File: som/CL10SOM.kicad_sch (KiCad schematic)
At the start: 54 parts, among them IC1 10CL025YU256C8G, J1 Conn_01x02_Pin, U1 MT46H32M16LFBF-5 IT:C, U2 MX25L12833FM2, U6 AT93C46DN-SH-T, U7 SG3225CAN 50.0000M-TJGA6, X1 DF40C-120DS-0.4V51

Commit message: Use switching regulators for 3v3 and 1v2
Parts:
- removed C24, C25, C27: 2.2uF, Capacitor_SMD:C_0603_1608Metric, symbol Sheet1-altium-import:root_0_C_0805
- removed J1: Conn_01x02_Pin, Library:JUMPER_1, symbol Connector:Conn_01x02_Pin
- removed VR1, VR5: AP7366EA-33W5-7, Library:SOT95P285X140-5N, symbol Library:AP7366EA-33W5-7
- removed VR2: AP7366EA-12W5-7, Library:SOT95P285X140-5N, symbol Library:AP7366EA-12W5-7
- added C1, C2: GRM21BR60J226ME39L, Library:CAPC2012X140N, symbol Library:GRM21BR60J226ME39L
- added L1, L2: MURATA_DFE21CCN1R0MELL, Library:MURATA_DFE21CCN1R0MELL_0, symbol Library:MURATA_DFE21CCN1R0MELL
- added TP1, TP2, TP3: TestPoint, TestPoint:TestPoint_THTPad_D1.5mm_Drill0.7mm, symbol Connector:TestPoint
- added U3: SC189ZSKTRT, Library:SOT23-5-SC189_SEM, symbol Library:SC189ZSKTRT
- added U4: SC189CSKTRT, Library:SOT_CSKTRT_SEM, symbol Library:SC189CSKTRT
- C26, C99: value 2.2uF -> 4.7uF
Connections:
- net +3.3V is gone; now on net +3V3: X1.109, X1.111
- net +1V2: now also C2.1, L2.2, U4.4 (VOUT(1.2V))
- net +3V3: now also C28.2, C29.2, VR3.1 (IN), VR3.3 (EN), VR4.1 (IN), VR4.3 (EN), X1.11, X1.13, X1.15, X1.17, C1.1, L1.2, TP3.1, U3.4 (VOUT(3.3V))
- net +5V: now also C26.2, X1.9, TP2.1, U3.1 (VIN), U3.3 (EN), U4.1 (VIN), U4.3 (EN); no longer C28.2, C29.2, VR3.1 (IN), VR3.3 (EN), VR4.1 (IN), VR4.3 (EN)
- net GND: now also C1.2, C2.2, TP1.1, U3.2 (GND), U4.2 (GND)
- net TCK: now also X1.12; no longer X1.10
- net TDI: now also X1.10; no longer X1.9
- net TDO: now also X1.16; no longer X1.12
- net TMS: now also X1.14; no longer X1.11
- new net: L1.1, U3.5 (LX)
- new net: L2.1, U4.5 (LX)
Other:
- moved on the sheet: C22, C23, C26, C28, C29, C99, VR3, VR4

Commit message: All routed, no errors
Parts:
- removed U7: SG3225CAN 50.0000M-TJGA6, Library:SG3225CAN, symbol Sheet1-altium-import:root_0_SG-310
- added C10, C19, C24, C25, C27: 100nF, Capacitor_SMD:C_0603_1608Metric, symbol Sheet1-altium-import:root_1_C_0805
- added TP4, TP5, TP6: TestPoint, TestPoint:TestPoint_THTPad_D1.5mm_Drill0.7mm, symbol Connector:TestPoint
- added U7, U8: SG3225CAN 50.0000M-TJGA6, Library:SG3225CAN, symbol Library:SG3225CAN
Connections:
- net B7-CLK9 is gone; now on net GND: IC1.B9 (CLK9/DIFFCLK_5p)
- net B8-CLK10 is gone; now on net GND: IC1.A8 (CLK10/DIFFCLK_4n)
- net B8-CLK11 is gone; now on net GND: IC1.B8 (CLK11/DIFFCLK_4p)
- net +1V2: now also TP4.1
- net +1V8: now also X1.113, X1.115, C10.2, TP6.1, U8.4 (VCC); no longer X1.117, X1.119
- net +2V5: now also X1.109, X1.111, X1.17, TP5.1; no longer X1.113, X1.115
- net +3V3: now also X1.117, X1.119, X1.9, U7.4 (VCC); no longer X1.109, X1.111, X1.17
- net +5V: no longer X1.9
- net B3-IO15: no longer IC1.N8 (IO/DIFFIO_B11p), X1.54
- net B3-IO16: now also IC1.N8 (IO/DIFFIO_B11p), X1.54; no longer IC1.P8 (IO/DIFFIO_B12n), X1.56
- net CLC50: now also U7.3 (OUT)
- net GND: now also C10.1, C19.2, C24.2, C25.2, C27.2, U7.2 (GND), U8.2 (GND)
- net VCCB2: now also C19.1
- net VCCB3: now also C24.1
- net VCCB4: now also C25.1
- net VCCB5: now also C27.1
- net B7-CLK8 renamed CLCOPT
- net CLCOPT: now also U8.3 (OUT)
- new net B3-IO17: IC1.P8 (IO/DIFFIO_B12n), X1.56
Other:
- moved on the sheet: TP3

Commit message: Fixed warnings
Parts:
- removed TP2: TestPoint, TestPoint:TestPoint_THTPad_D1.5mm_Drill0.7mm, symbol Connector:TestPoint
- TP1, TP3, TP4, TP5, TP6: footprint TestPoint:TestPoint_THTPad_D1.5mm_Drill0.7mm -> TestPoint:TestPoint_THTPad_D1.0mm_Drill0.5mm
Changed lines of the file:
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@@
 	(wire
 		(pts
-			(xy 69.85 153.67) (xy 69.85 158.75)
-		)
-		(stroke
-			(width 0)
-			(type default)
-		)
-	)
-	(wire
-		(pts
 			(xy 203.2 378.46) (xy 203.2 379.73)
 		)
@@
 	(wire
 		(pts
-			(xy 55.88 153.67) (xy 55.88 158.75)
-		)
-		(stroke
-			(width 0)
-			(type default)
-		)
-	)
-	(wire
-		(pts
 			(xy 46.99 86.36) (xy 36.83 86.36)
 		)
@@
 	)
 	(symbol
-		(lib_id "Connector:TestPoint")
-		(at 55.88 158.75 180)
-		(unit 1)
-		(exclude_from_sim no)
-		(in_bom yes)
-		(on_board yes)
-		(dnp no)
-		(fields_autoplaced yes)
-		(property "Reference" "TP2"
-			(at 58.42 160.7819 0)
-			(effects
-				(font
-					(size 1.27 1.27)
-				)
-				(justify right)
-			)
-		)
-		(property "Value" "TestPoint"
-			(at 58.42 163.3219 0)
-			(effects
-				(font
-					(size 1.27 1.27)
-				)
-				(justify right)
-			)
-		)
-		(property "Footprint" "TestPoint:TestPoint_THTPad_D1.5mm_Drill0.7mm"
-			(at 50.8 158.75 0)
-			(effects
-				(font
-					(size 1.27 1.27)
-				)
-				(hide yes)
-			)
-		)
-		(property "Datasheet" "~"
-			(at 50.8 158.75 0)
-			(effects
-				(font
-					(size 1.27 1.27)
-				)
-				(hide yes)
-			)
-		)
-		(property "Description" "test point"
-			(at 55.88 158.75 0)
-			(effects
-				(font
-					(size 1.27 1.27)
-				)
-				(hide yes)
-			)
-		)
-		(pin "1"
-		)
-		(instances
-			(project ""
-				(path "/dc7b2672-e830-4a16-8d9e-d44ab4cff2d4"
-					(reference "TP2")
-					(unit 1)
-				)
-			)
-		)
-	)
-	(symbol
 		(lib_id "Sheet1-altium-import:root_1_C_0805")
 		(at 457.2 359.41 0)
@@
 			)
 		)
-		(property "Footprint" "TestPoint:TestPoint_THTPad_D1.5mm_Drill0.7mm"
+		(property "Footprint" "TestPoint:TestPoint_THTPad_D1.0mm_Drill0.5mm"
 			(at 45.72 154.94 0)
 			(effects
@@
 			)
 		)
-		(property "Footprint" "TestPoint:TestPoint_THTPad_D1.5mm_Drill0.7mm"
+		(property "Footprint" "TestPoint:TestPoint_THTPad_D1.0mm_Drill0.5mm"
 			(at 81.28 101.6 0)
 			(effects
@@
 	)
 	(symbol
-		(lib_id "power:+5V")
-		(at 55.88 153.67 0)
-		(unit 1)
-		(exclude_from_sim no)
-		(in_bom yes)
-		(on_board yes)
-		(dnp no)
-		(fields_autoplaced yes)
-		(property "Reference" "#PWR051"
-			(at 55.88 157.48 0)
-			(effects
-				(font
-					(size 1.27 1.27)
-				)
-				(hide yes)
-			)
-		)
-		(property "Value" "+5V"
-			(at 55.88 148.59 0)
-			(effects
-				(font
-					(size 1.27 1.27)
-				)
-			)
-		)
-		(property "Footprint" ""
-			(at 55.88 153.67 0)
-			(effects
-				(font
-					(size 1.27 1.27)
-				)
-				(hide yes)
-			)
-		)
-		(property "Datasheet" ""
-			(at 55.88 153.67 0)
-			(effects
-				(font
-					(size 1.27 1.27)
-				)
-				(hide yes)
-			)
-		)
-		(property "Description" "Power symbol creates a global label with name \"+5V\""
-			(at 55.88 153.67 0)
-			(effects
-				(font
-					(size 1.27 1.27)
-				)
-				(hide yes)
-			)
-		)
-		(pin "1"
-		)
-		(instances
-			(project "HyperFusionXC"
-				(path "/dc7b2672-e830-4a16-8d9e-d44ab4cff2d4"
-					(reference "#PWR051")
-					(unit 1)
-				)
-			)
-		)
-	)
-	(symbol
 		(lib_id "Sheet1-altium-import:root_1_C_0805")
 		(at 274.32 85.09 0)
@@
 			)
 		)
-		(property "Footprint" "TestPoint:TestPoint_THTPad_D1.5mm_Drill0.7mm"
+		(property "Footprint" "TestPoint:TestPoint_THTPad_D1.0mm_Drill0.5mm"
 			(at 128.27 41.91 0)
 			(effects
@@
 			)
 		)
-		(property "Footprint" "TestPoint:TestPoint_THTPad_D1.5mm_Drill0.7mm"
+		(property "Footprint" "TestPoint:TestPoint_THTPad_D1.0mm_Drill0.5mm"
 			(at 129.54 73.66 0)
 			(effects
@@
 			)
 		)
-		(property "Footprint" "TestPoint:TestPoint_THTPad_D1.5mm_Drill0.7mm"
+		(property "Footprint" "TestPoint:TestPoint_THTPad_D1.0mm_Drill0.5mm"
 			(at 81.28 127 0)
 			(effects

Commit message: Improvements
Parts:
- H1: footprint MountingHole:MountingHole_3.5mm_Pad_Via -> MountingHole:MountingHole_2.7mm_M2.5_Pad_Via
- IC1: footprint BGA256C80P16X16_1400X1400X150 -> Library:BGA256C80P16X16_1400X1400X150
- U1: footprint MIC-VFBGA-60-BF_MRN -> Library:MIC-VFBGA-60-BF_MRN
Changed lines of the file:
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@@
 			)
 		)
-		(property "Footprint" "MountingHole:MountingHole_3.5mm_Pad_Via"
+		(property "Footprint" "MountingHole:MountingHole_2.7mm_M2.5_Pad_Via"
 			(at 558.8 359.41 0)
 			(effects
@@
 			)
 		)
-		(property "Footprint" "MIC-VFBGA-60-BF_MRN"
+		(property "Footprint" "Library:MIC-VFBGA-60-BF_MRN"
 			(at 440.69 105.41 0)
 			(effects
@@
 			)
 		)
-		(property "Footprint" "BGA256C80P16X16_1400X1400X150"
+		(property "Footprint" "Library:BGA256C80P16X16_1400X1400X150"
 			(at 162.56 205.41 0)
 			(effects

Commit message: Improvements
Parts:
- C1, C2: LCSC (none) -> C77071
- C10: now not fitted
- C12, C13, C14, C15, C16, C17, C18, C19, C20, C21, C24, C25, C27, C30, C37, C38, C39, C40, C41, C42, C43, C45, C7, C9: LCSC (none) -> C45000
- C22, C23, C28, C29: LCSC (none) -> C100082
- C26, C99: DIGIKEY 1276-1134-1-ND -> 1276-2087-1-ND; LCSC (none) -> C107368
- IC1: LCSC (none) -> C1521917
- L1, L2: value MURATA_DFE21CCN1R0MELL -> DFE21CCN1R0MELL; LCSC (none) -> C3221768
- R44, R68: LCSC (none) -> C3029194
- R46, R47, R48, R49, R56, R58, R59, R60: LCSC (none) -> C238881
- R57: LCSC (none) -> C2484712
- R62: value 25E -> 24E9; DIGIKEY RMCF0603FT1K00CT-ND -> 311-24.9HRCT-ND; LCSC (none) -> C137759
- U1: LCSC (none) -> C2061960
- U2: LCSC (none) -> C701355
- U3: LCSC (none) -> C2650317
- U4: LCSC (none) -> C783594
- U6: LCSC (none) -> C6499
- U7: LCSC (none) -> C17330697
- U8: LCSC (none) -> C17330697; now not fitted
- X1: LCSC (none) -> C3647197

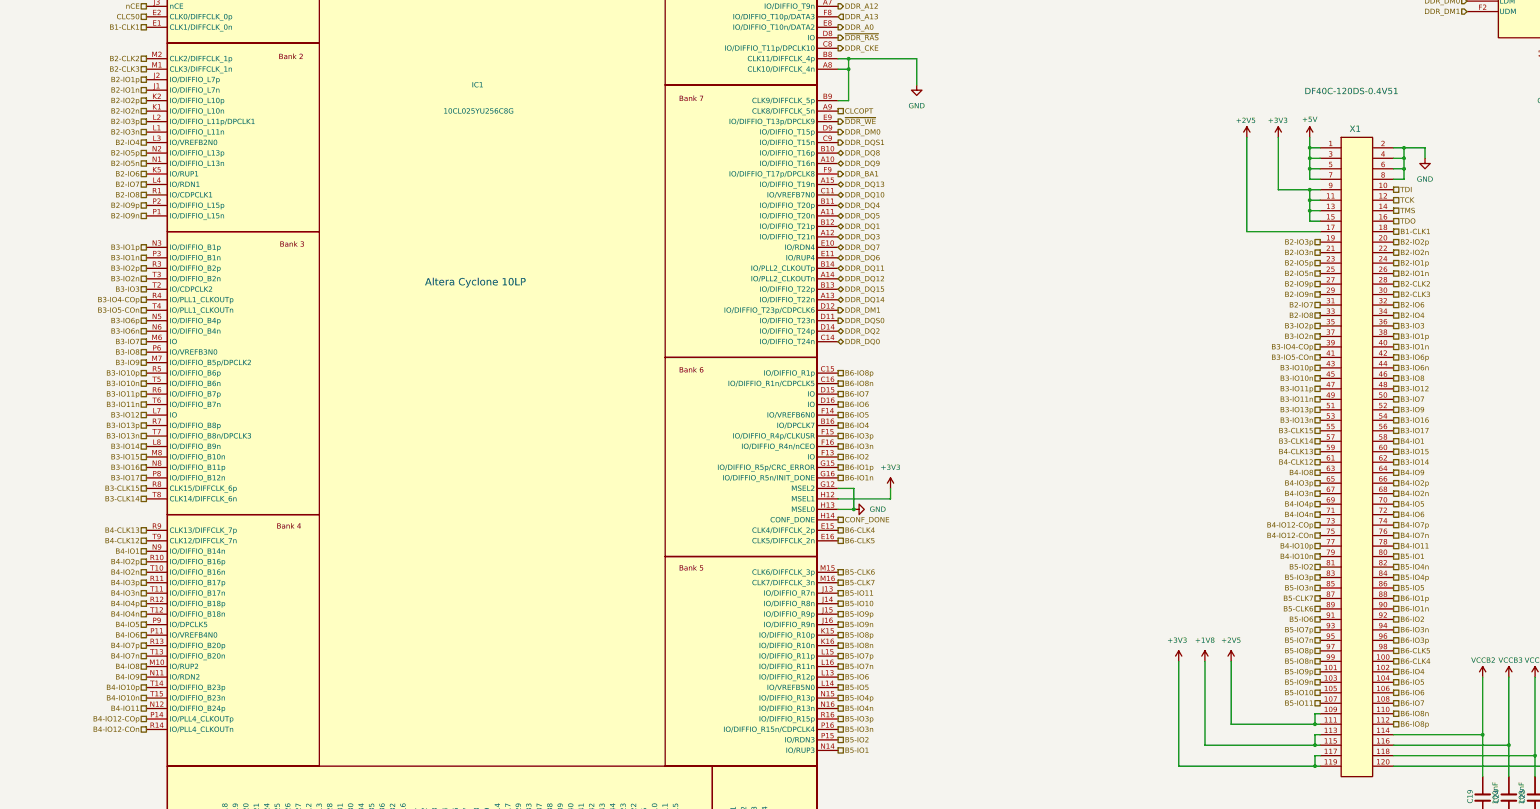
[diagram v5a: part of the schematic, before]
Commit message: Use differential routing
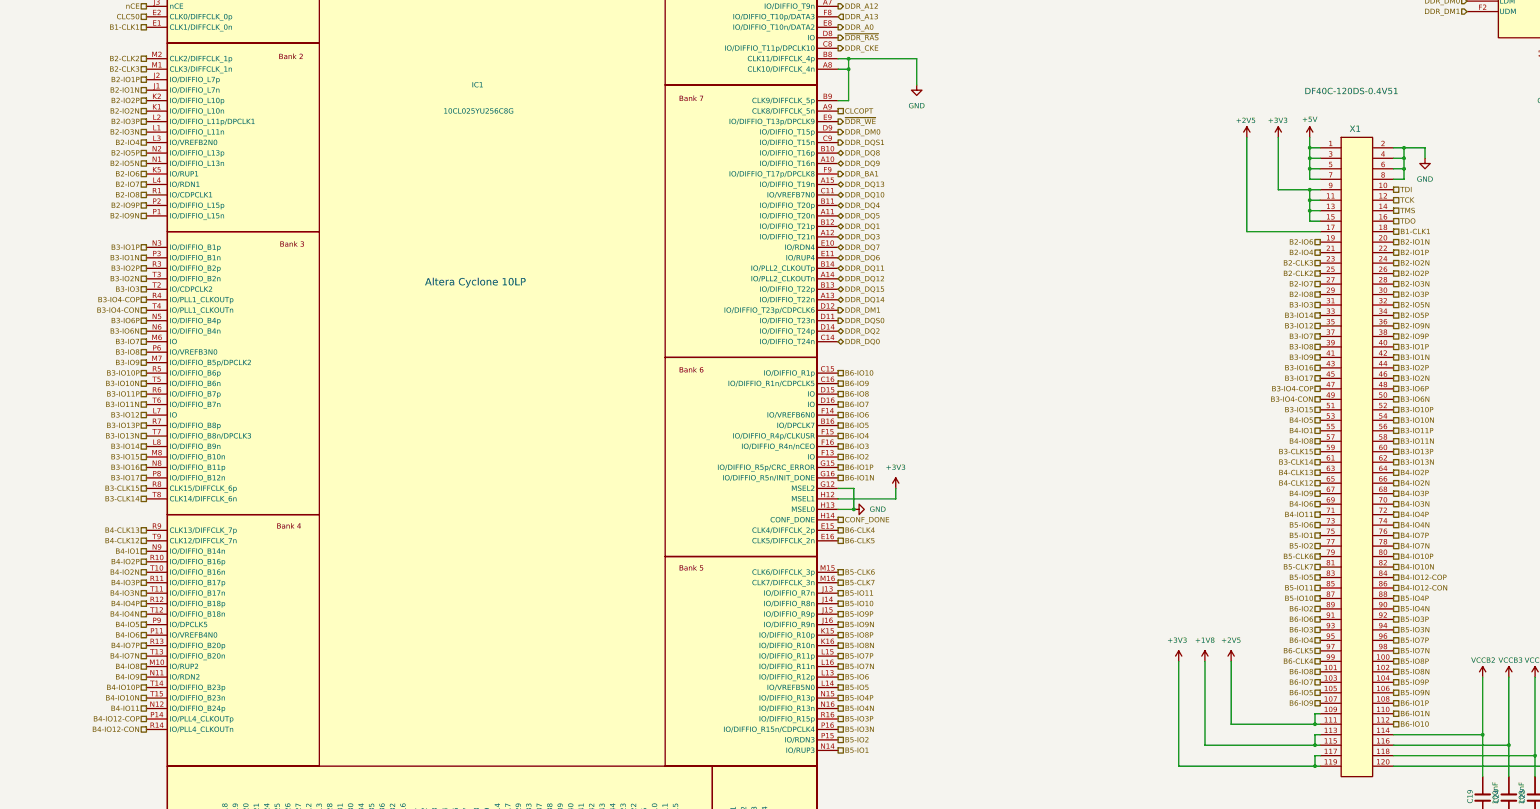
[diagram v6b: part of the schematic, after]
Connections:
- net B2-CLK2: now also X1.25; no longer X1.28
- net B2-CLK3: now also X1.23; no longer X1.30
- net B2-IO4: now also X1.21; no longer X1.34
- net B2-IO6: now also X1.19; no longer X1.32
- net B2-IO7: now also X1.27; no longer X1.31
- net B2-IO8: now also X1.29; no longer X1.33
- net B3-CLK14: now also X1.61; no longer X1.57
- net B3-CLK15: now also X1.59; no longer X1.55
- net B3-IO12: now also X1.35; no longer X1.48
- net B3-IO14: now also X1.33; no longer X1.62
- net B3-IO15: now also X1.51; no longer X1.60
- net B3-IO16: now also X1.43; no longer X1.54
- net B3-IO17: now also X1.45; no longer X1.56
- net B3-IO3: now also X1.31; no longer X1.36
- net B3-IO7: now also X1.37; no longer X1.50
- net B3-IO8: now also X1.39; no longer X1.46
- net B3-IO9: now also X1.41; no longer X1.52
- net B4-CLK12: now also X1.65; no longer X1.61
- net B4-CLK13: now also X1.63; no longer X1.59
- net B4-IO1: now also X1.55; no longer X1.58
- net B4-IO11: now also X1.71; no longer X1.78
- net B4-IO5: now also X1.53; no longer X1.70
- net B4-IO6: now also X1.69; no longer X1.72
- net B4-IO8: now also X1.57; no longer X1.63
- net B4-IO9: now also X1.67; no longer X1.64
- net B5-CLK6: now also X1.79; no longer X1.89
- net B5-CLK7: now also X1.81; no longer X1.87
- net B5-IO1: now also X1.75; no longer X1.80
- net B5-IO10: now also X1.87; no longer X1.105
- net B5-IO11: now also X1.85; no longer X1.107
- net B5-IO2: now also X1.77; no longer X1.81
- net B5-IO5: now also X1.83; no longer X1.86
- net B5-IO6: now also X1.73; no longer X1.91
- net B6-CLK4: now also X1.99; no longer X1.100
- net B6-CLK5: now also X1.97; no longer X1.98
- net B6-IO2: now also X1.89; no longer X1.92
- net B6-IO4: now also IC1.F15 (IO/DIFFIO_R4p/CLKUSR), X1.95; no longer IC1.B16 (IO/DPCLK7), X1.102
- net B6-IO5: now also IC1.B16 (IO/DPCLK7), X1.105; no longer IC1.F14 (IO/VREFB6N0), X1.104
- net B6-IO6: now also IC1.F14 (IO/VREFB6N0), X1.91; no longer IC1.D16 (IO), X1.106
- net B6-IO7: now also IC1.D16 (IO), X1.103; no longer IC1.D15 (IO), X1.108
- net B2-IO1n renamed B2-IO1N
- net B2-IO1N: now also X1.20; no longer X1.26
- net B2-IO1p renamed B2-IO1P
- net B2-IO1P: now also X1.22; no longer X1.24
- net B2-IO2n renamed B2-IO2N
- net B2-IO2N: now also X1.24; no longer X1.22
- net B2-IO2p renamed B2-IO2P
- net B2-IO2P: now also X1.26; no longer X1.20
- net B2-IO3n renamed B2-IO3N
- net B2-IO3N: now also X1.28; no longer X1.21
- net B2-IO3p renamed B2-IO3P
- net B2-IO3P: now also X1.30; no longer X1.19
- net B2-IO5n renamed B2-IO5N
- net B2-IO5N: now also X1.32; no longer X1.25
- net B2-IO5p renamed B2-IO5P
- net B2-IO5P: now also X1.34; no longer X1.23
- net B2-IO9n renamed B2-IO9N
- net B2-IO9N: now also X1.36; no longer X1.29
- net B2-IO9p renamed B2-IO9P
- net B2-IO9P: now also X1.38; no longer X1.27
- net B3-IO10n renamed B3-IO10N
- net B3-IO10N: now also X1.54; no longer X1.45
- net B3-IO10p renamed B3-IO10P
- net B3-IO10P: now also X1.52; no longer X1.43
- net B3-IO11n renamed B3-IO11N
- net B3-IO11N: now also X1.58; no longer X1.49
- net B3-IO11p renamed B3-IO11P
- net B3-IO11P: now also X1.56; no longer X1.47
- net B3-IO13n renamed B3-IO13N
- net B3-IO13N: now also X1.62; no longer X1.53
- net B3-IO13p renamed B3-IO13P
- net B3-IO13P: now also X1.60; no longer X1.51
- net B3-IO1n renamed B3-IO1N
- net B3-IO1N: now also X1.42; no longer X1.40
- net B3-IO1p renamed B3-IO1P
- net B3-IO1P: now also X1.40; no longer X1.38
- net B3-IO2n renamed B3-IO2N
- net B3-IO2N: now also X1.46; no longer X1.37
- net B3-IO2p renamed B3-IO2P
- net B3-IO2P: now also X1.44; no longer X1.35
- net B3-IO4-COp renamed B3-IO4-COP
- net B3-IO4-COP: now also X1.47; no longer X1.39
- net B3-IO5-COn renamed B3-IO4-CON
- net B3-IO4-CON: now also X1.49; no longer X1.41
- net B3-IO6n renamed B3-IO6N
- net B3-IO6N: now also X1.50; no longer X1.44
- net B3-IO6p renamed B3-IO6P
- net B3-IO6P: now also X1.48; no longer X1.42
- net B4-IO10n renamed B4-IO10N
- net B4-IO10N: now also X1.82; no longer X1.79
- net B4-IO10p renamed B4-IO10P
- net B4-IO10P: now also X1.80; no longer X1.77
- net B4-IO12-COn renamed B4-IO12-CON
- net B4-IO12-CON: now also X1.86; no longer X1.75
- net B4-IO12-COp renamed B4-IO12-COP
- net B4-IO12-COP: now also X1.84; no longer X1.73
- net B4-IO2n renamed B4-IO2N
- net B4-IO2N: now also X1.66; no longer X1.68
- net B4-IO2p renamed B4-IO2P
- net B4-IO2P: now also X1.64; no longer X1.66
- net B4-IO3n renamed B4-IO3N
- net B4-IO3N: now also X1.70; no longer X1.67
- net B4-IO3p renamed B4-IO3P
- net B4-IO3P: now also X1.68; no longer X1.65
- net B4-IO4n renamed B4-IO4N
- net B4-IO4N: now also X1.74; no longer X1.71
- net B4-IO4p renamed B4-IO4P
- net B4-IO4P: now also X1.72; no longer X1.69
- net B4-IO7n renamed B4-IO7N
- net B4-IO7N: now also X1.78; no longer X1.76
- net B4-IO7p renamed B4-IO7P
- net B4-IO7P: now also X1.76; no longer X1.74
- net B5-IO3n renamed B5-IO3N
- net B5-IO3N: now also X1.94; no longer X1.85
- net B5-IO3p renamed B5-IO3P
- net B5-IO3P: now also X1.92; no longer X1.83
- net B5-IO4n renamed B5-IO4N
- net B5-IO4N: now also X1.90; no longer X1.82
- net B5-IO4p renamed B5-IO4P
- net B5-IO4P: now also X1.88; no longer X1.84
- net B5-IO7n renamed B5-IO7N
- net B5-IO7N: now also X1.98; no longer X1.95
- net B5-IO7p renamed B5-IO7P
- net B5-IO7P: now also X1.96; no longer X1.93
- net B5-IO8n renamed B5-IO8N
- net B5-IO8N: now also X1.102; no longer X1.99
- net B5-IO8p renamed B5-IO8P
- net B5-IO8P: now also X1.100; no longer X1.97
- net B5-IO9n renamed B5-IO9N
- net B5-IO9N: now also X1.106; no longer X1.103
- net B5-IO9p renamed B5-IO9P
- net B5-IO9P: now also X1.104; no longer X1.101
- net B6-IO1n renamed B6-IO1N
- net B6-IO1N: now also X1.110; no longer X1.90
- net B6-IO1p renamed B6-IO1P
- net B6-IO1P: now also X1.108; no longer X1.88
- net B6-IO3n renamed B6-IO3
- net B6-IO3: now also X1.93; no longer X1.94
- removed net B6-IO3p: IC1.F15 (IO/DIFFIO_R4p/CLKUSR), X1.96
- net B6-IO8n renamed B6-IO9
- net B6-IO9: now also X1.107; no longer X1.110
- net B6-IO8p renamed B6-IO10
- new net B6-IO8: IC1.D15 (IO), X1.101
